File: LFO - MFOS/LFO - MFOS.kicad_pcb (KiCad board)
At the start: 2 copper layers, 101.6 x 101.6 mm, 102 parts, among them J1 CFV, J10 PWXY, J11 PWC, J12 SIN, J13 PW10, J14 PW90, J15 SQR, J16 LEDA, J17 +12V_Conn, J18 GND_Conn, J19 -12V_Conn, J2 CV1, J3 CV2, J4 CV3, J5 CFL, J6 FFV, J7 TRI, J8 RMP, J9 SAW, Q1 Q_NJFET_DSG, Q2 Q_NJFET_DSG, Q3 2N3904, Q4 2N3904, Q5 2N3906, Q6 2N3904, U1 LM13700, U2 TL082, U3 TL082, U4 TL072, U5 TL082, U6 TL082

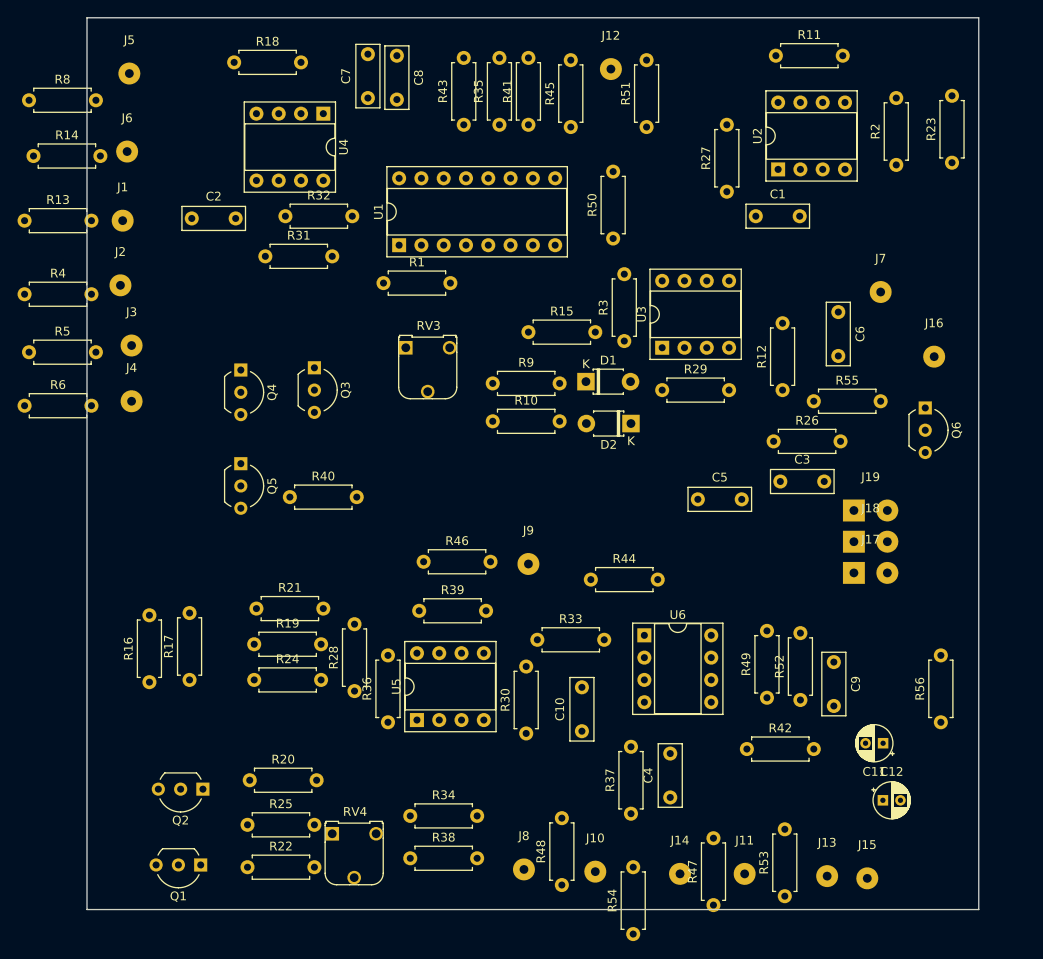
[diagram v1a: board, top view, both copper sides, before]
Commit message: added functional silkscreen
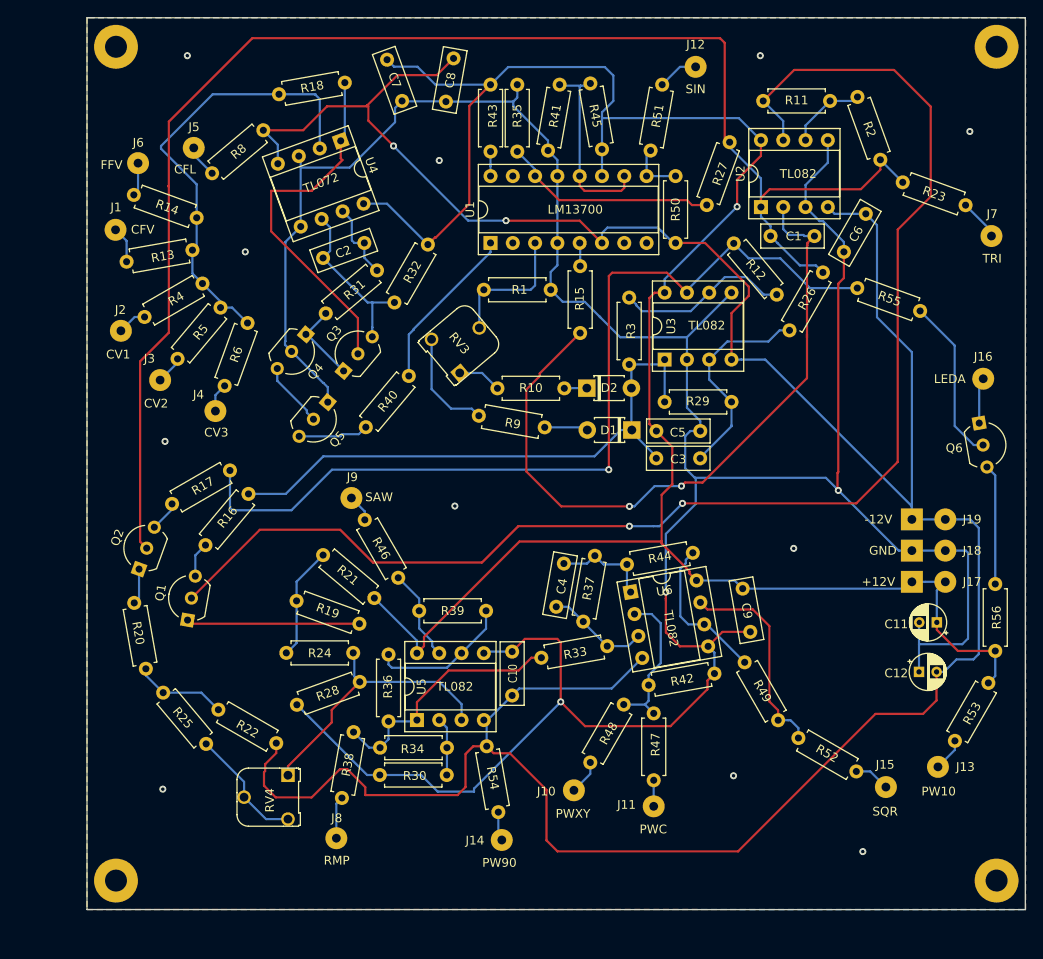
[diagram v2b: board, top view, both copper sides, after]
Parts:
- added REF**: MountingHole_2.5mm_Pad, MountingHole:MountingHole_2.5mm_Pad, F.Cu at (15.5, 110.5)
- added REF**: MountingHole_2.5mm_Pad, MountingHole:MountingHole_2.5mm_Pad, F.Cu at (115.8, 110.5)
- added REF**: MountingHole_2.5mm_Pad, MountingHole:MountingHole_2.5mm_Pad, F.Cu at (115.8, 15.5)
- added REF**: MountingHole_2.5mm_Pad, MountingHole:MountingHole_2.5mm_Pad, F.Cu at (15.5, 15.5)
- moved R53 33.6 mm to (114.9, 88.0), turned to 240 degrees
- moved R37 29.7 mm to (70.1, 73.5), turned to 260 degrees
- moved C4 29.3 mm to (66.5, 74.4), turned to 260 degrees
- moved Q1 27.9 mm to (23.6, 80.8), turned to 80 degrees
- moved R6 27.1 mm to (30.5, 47.0), turned to 250 degrees
- moved R8 26.9 mm to (32.3, 25.0), turned to 220 degrees
- moved Q2 26.1 mm to (18.1, 75.0), turned to 70 degrees
- moved R47 22.9 mm to (76.8, 91.4), turned to 270 degrees
- moved R5 22.4 mm to (27.4, 45.2), turned to 230 degrees
- moved R48 21.7 mm to (73.3, 90.4), turned to 240 degrees
- moved J8 21.7 mm to (40.6, 105.7)
- moved J9 21.5 mm to (42.3, 66.9), turned to 30 degrees
- moved R54 20.7 mm to (59.1, 102.7), turned to 100 degrees
- moved J14 20.7 mm to (59.4, 105.9)
- moved R4 20.3 mm to (25.3, 42.5), turned to 210 degrees
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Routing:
- net Earth: track 0.00 -> 338.5 mm, vias 0 -> 3
- net -12V: track 0.00 -> 325.4 mm, vias 0 -> 2
- net +12V: track 0.00 -> 237.7 mm, vias 0 -> 1
- net Net-(C1-Pad1): track 0.00 -> 170.5 mm
- net Net-(Q1-Pad2): track 0.00 -> 159.7 mm, vias 0 -> 2
- net ZZ: track 0.00 -> 105.5 mm, vias 0 -> 1
- net Net-(C1-Pad2): track 0.00 -> 81.3 mm, vias 0 -> 2
- net Net-(C3-Pad1): track 0.00 -> 67.6 mm
- net Net-(R13-Pad1): track 0.00 -> 51.8 mm
- net Net-(Q3-Pad2): track 0.00 -> 41.3 mm
- net Net-(R24-Pad1): track 0.00 -> 32.1 mm
- net Net-(R33-Pad1): track 0.00 -> 28.8 mm
- net Net-(C3-Pad2): track 0.00 -> 24.2 mm
- net Net-(R27-Pad1): track 0.00 -> 24.0 mm
- net Net-(R49-Pad2): track 0.00 -> 23.9 mm
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- added copper zone on B.Cu, net Earth
- added copper zone on F.Cu, net Earth
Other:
- board size 101.6 x 101.6 mm -> 106.9 x 101.6 mm
- net class Default: clearance 0.2 -> 0.5
- rule trace_clearance: 0.2 -> 0.5
- rule via_min_size: 0.4 -> 0.6
- board text added: "+12V"
- board text added: "-12V"
- board text added: "CFL"
- board text added: "CFV"
- board text added: "CV1"
- board text added: "CV2"
- board text added: "CV3"
- board text added: "FFV"
- board text added: "GND"
- board text added: "LEDA"
- board text added: "LM13700"
- board text added: "PW10"
- board text added: "PW90"
- board text added: "PWC"
- board text added: "PWXY"
- board text added: "RMP"
- board text added: "SAW"
- board text added: "SIN"
- board text added: "SQR"
- board text added: "TL072"
- board text added: "TL082"
- board text added: "TRI"

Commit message: made silkscreen pretty
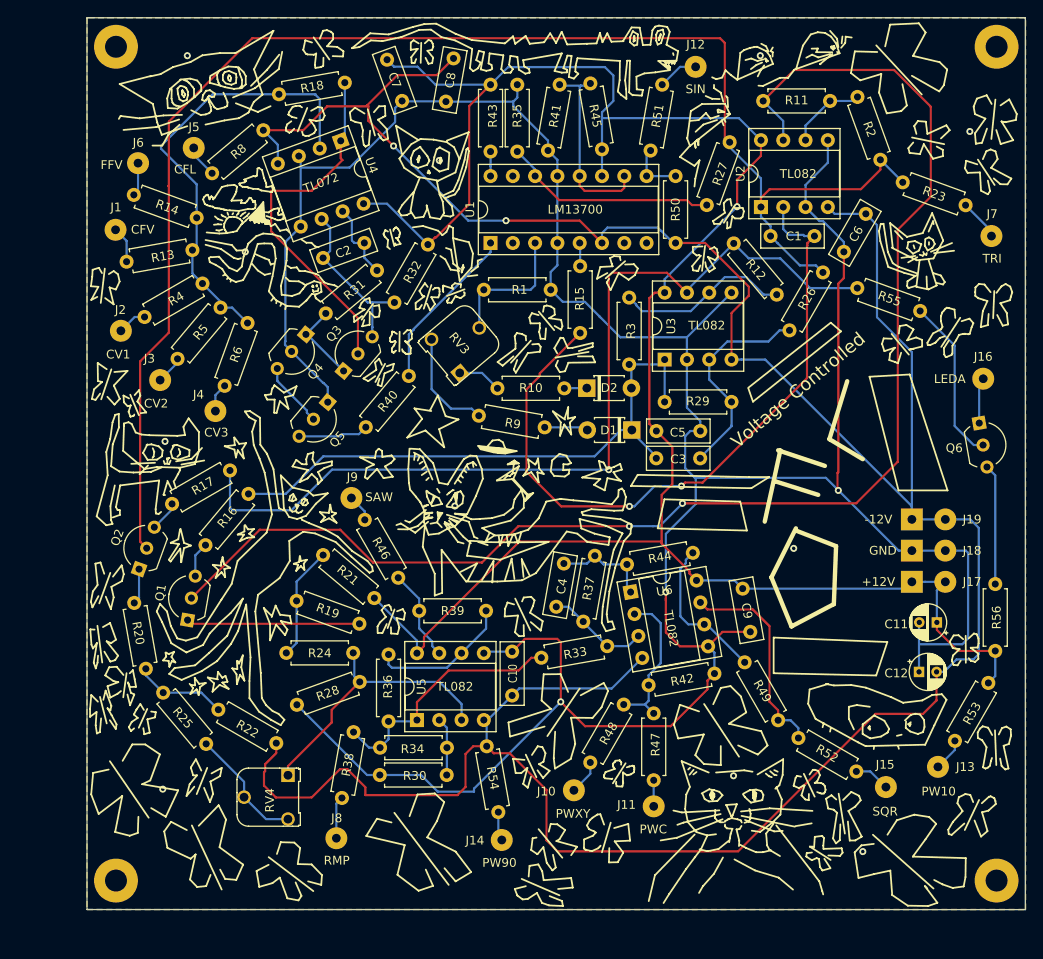
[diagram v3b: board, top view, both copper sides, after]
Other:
- board text added: "Voltage Controlled"
